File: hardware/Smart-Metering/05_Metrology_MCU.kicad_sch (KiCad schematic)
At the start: 26 parts, among them J501 SWD, U501 STM32F413RHT6, Y501 8MHz, Y502 32.768kHz

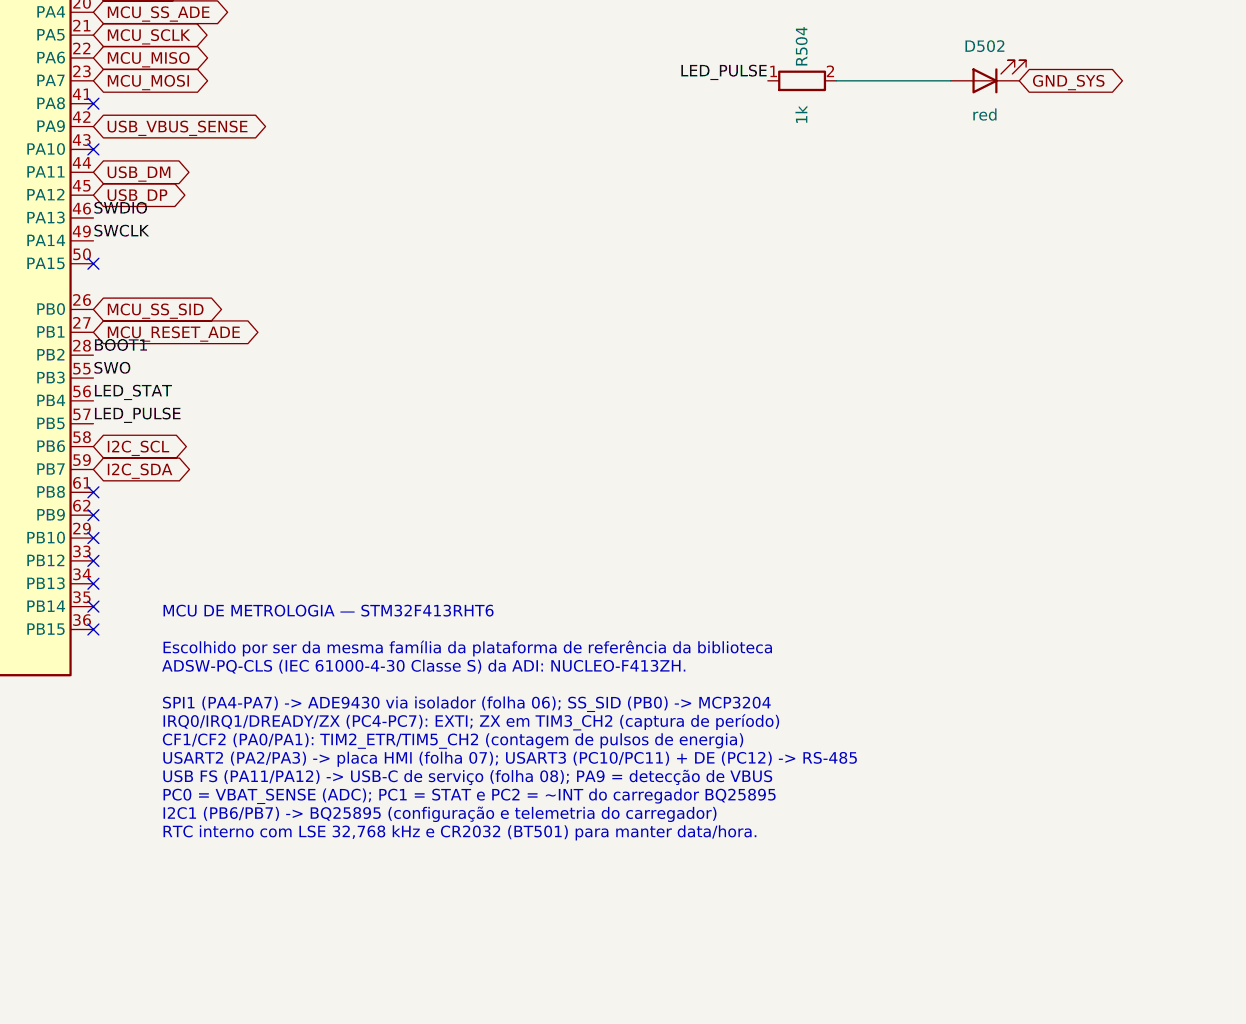
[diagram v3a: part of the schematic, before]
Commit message: Resolve as pendências da revisão do esquemático
P1  ADE9430: footprint VQFN-40 6x6 com EP de 4,15 mm, compatível com as
    variantes CP-40 de 6x6 mm (EP de 3,9 a 4,7 mm).
P2  Confirmado no datasheet: MISO solto com SS alto (pull-up de 100 kΩ)
    e NC1/NC2 em GND, como já estava.
P3  J301-J304: headers JST PH de 4 vias cabeados até conectores M8
    fêmea de painel (à prova de toque).
P4  PS601 -> U606 ADuM6000 (isoPower 5 kVrms, símbolo oficial).
P5  PS101 -> RAC20-05SK/277 (85-305 VAC, 120-430 VDC, 20 W); fusíveis
    T500mA, R101 3 W, C101 10 uF/450 V; entrada do BQ25895 a 3 A.
P7  TPS61089 -> TPS61022 (compensação interna, sem valores a ajustar).
P8  Placa EV alimentada pelos pinos 5 V do J1 (nota na folha 07).
P9  EEPROM de calibração 24LC64 no I2C1.
P10 Labels globais de uma só folha convertidos em locais.

Verificação: 223 componentes, nenhum pino solto, nenhuma net sem fonte,
nenhum conflito de saída, isolação íntegra, todos os footprints
existentes na biblioteca oficial do KiCad.

Co-Authored-By: Claude Opus 5.5 <noreply@anthropic.com>
Claude-Session: https://claude.ai/code/session_012B8cVkhtjf3eg98UdpNCpf
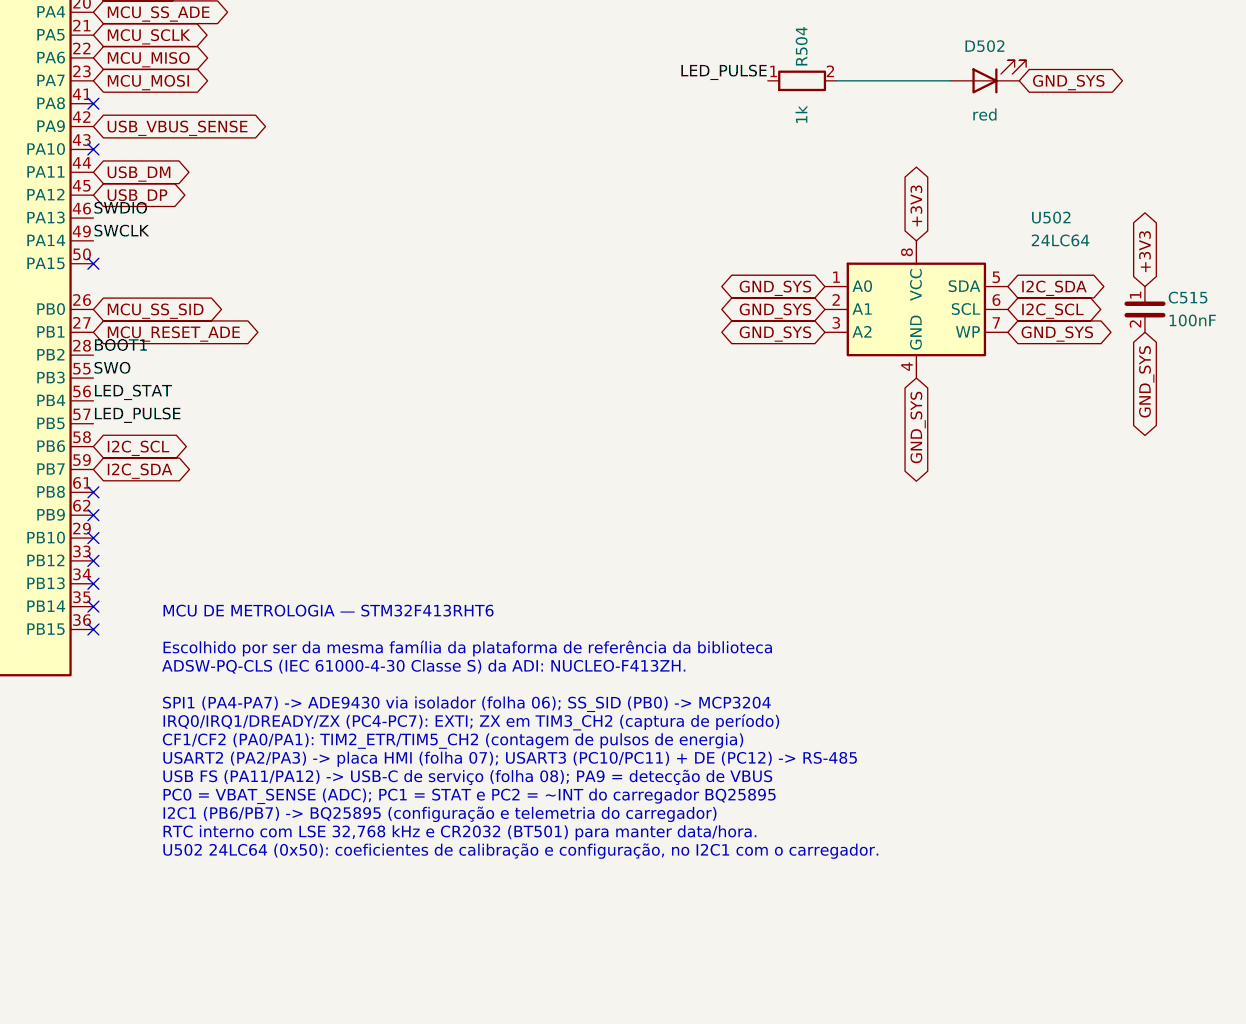
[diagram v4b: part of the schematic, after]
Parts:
- added C515: 100nF, Capacitor_SMD:C_0603_1608Metric, symbol SmartMetering:C_Vert
- added U502: 24LC64, Package_SO:SOIC-8_3.9x4.9mm_P1.27mm, symbol Memory_EEPROM:24LC64
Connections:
- net +3V3: now also C515.1, U502.8 (VCC)
- net GND_SYS: now also C515.2, U502.1 (A0), U502.2 (A1), U502.3 (A2), U502.4 (GND), U502.7 (WP)
- net I2C_SCL: now also U502.6 (SCL)
- net I2C_SDA: now also U502.5 (SDA)
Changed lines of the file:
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@@
 		(comment 2 "Platform matches the ADSW-PQ-CLS reference (NUCLEO-F413ZH)")
 	)
-	(text "MCU DE METROLOGIA — STM32F413RHT6\n\nEscolhido por ser da mesma família da plataforma de referência da biblioteca\nADSW-PQ-CLS (IEC 61000-4-30 Classe S) da ADI: NUCLEO-F413ZH.\n\nSPI1 (PA4-PA7) -> ADE9430 via isolador (folha 06); SS_SID (PB0) -> MCP3204\nIRQ0/IRQ1/DREADY/ZX (PC4-PC7): EXTI; ZX em TIM3_CH2 (captura de período)\nCF1/CF2 (PA0/PA1): TIM2_ETR/TIM5_CH2 (contagem de pulsos de energia)\nUSART2 (PA2/PA3) -> placa HMI (folha 07); USART3 (PC10/PC11) + DE (PC12) -> RS-485\nUSB FS (PA11/PA12) -> USB-C de serviço (folha 08); PA9 = detecção de VBUS\nPC0 = VBAT_SENSE (ADC); PC1 = STAT e PC2 = ~INT do carregador BQ25895\nI2C1 (PB6/PB7) -> BQ25895 (configuração e telemetria do carregador)\nRTC interno com LSE 32,768 kHz e CR2032 (BT501) para manter data/hora."
+	(text "MCU DE METROLOGIA — STM32F413RHT6\n\nEscolhido por ser da mesma família da plataforma de referência da biblioteca\nADSW-PQ-CLS (IEC 61000-4-30 Classe S) da ADI: NUCLEO-F413ZH.\n\nSPI1 (PA4-PA7) -> ADE9430 via isolador (folha 06); SS_SID (PB0) -> MCP3204\nIRQ0/IRQ1/DREADY/ZX (PC4-PC7): EXTI; ZX em TIM3_CH2 (captura de período)\nCF1/CF2 (PA0/PA1): TIM2_ETR/TIM5_CH2 (contagem de pulsos de energia)\nUSART2 (PA2/PA3) -> placa HMI (folha 07); USART3 (PC10/PC11) + DE (PC12) -> RS-485\nUSB FS (PA11/PA12) -> USB-C de serviço (folha 08); PA9 = detecção de VBUS\nPC0 = VBAT_SENSE (ADC); PC1 = STAT e PC2 = ~INT do carregador BQ25895\nI2C1 (PB6/PB7) -> BQ25895 (configuração e telemetria do carregador)\nRTC interno com LSE 32,768 kHz e CR2032 (BT501) para manter data/hora.\nU502 24LC64 (0x50): coeficientes de calibração e configuração, no I2C1 com o carregador."
 		(exclude_from_sim no)(at 180.34 175.26 0)
 		(effects (font (size 1.27 1.27)) (justify left top))
@@
 		(effects (font (size 1.27 1.27)) (justify left))
 		(property "Intersheetrefs" "${INTERSHEET_REFS}" (at 275.59 116.84 0) (hide yes) (effects (font (size 1.27 1.27))))
+	)
+	(global_label "GND_SYS" (shape bidirectional) (at 254 139.7 180)
+		(effects (font (size 1.27 1.27)) (justify right))
+		(property "Intersheetrefs" "${INTERSHEET_REFS}" (at 254 139.7 0) (hide yes) (effects (font (size 1.27 1.27))))
+	)
+	(global_label "GND_SYS" (shape bidirectional) (at 254 142.24 180)
+		(effects (font (size 1.27 1.27)) (justify right))
+		(property "Intersheetrefs" "${INTERSHEET_REFS}" (at 254 142.24 0) (hide yes) (effects (font (size 1.27 1.27))))
+	)
+	(global_label "GND_SYS" (shape bidirectional) (at 254 144.78 180)
+		(effects (font (size 1.27 1.27)) (justify right))
+		(property "Intersheetrefs" "${INTERSHEET_REFS}" (at 254 144.78 0) (hide yes) (effects (font (size 1.27 1.27))))
+	)
+	(global_label "GND_SYS" (shape bidirectional) (at 264.16 149.86 270)
+		(effects (font (size 1.27 1.27)) (justify right))
+		(property "Intersheetrefs" "${INTERSHEET_REFS}" (at 264.16 149.86 0) (hide yes) (effects (font (size 1.27 1.27))))
+	)
+	(global_label "GND_SYS" (shape bidirectional) (at 274.32 144.78 0)
+		(effects (font (size 1.27 1.27)) (justify left))
+		(property "Intersheetrefs" "${INTERSHEET_REFS}" (at 274.32 144.78 0) (hide yes) (effects (font (size 1.27 1.27))))
+	)
+	(global_label "+3V3" (shape bidirectional) (at 264.16 134.62 90)
+		(effects (font (size 1.27 1.27)) (justify left))
+		(property "Intersheetrefs" "${INTERSHEET_REFS}" (at 264.16 134.62 0) (hide yes) (effects (font (size 1.27 1.27))))
+	)
+	(global_label "I2C_SDA" (shape bidirectional) (at 274.32 139.7 0)
+		(effects (font (size 1.27 1.27)) (justify left))
+		(property "Intersheetrefs" "${INTERSHEET_REFS}" (at 274.32 139.7 0) (hide yes) (effects (font (size 1.27 1.27))))
+	)
+	(global_label "I2C_SCL" (shape bidirectional) (at 274.32 142.24 0)
+		(effects (font (size 1.27 1.27)) (justify left))
+		(property "Intersheetrefs" "${INTERSHEET_REFS}" (at 274.32 142.24 0) (hide yes) (effects (font (size 1.27 1.27))))
+	)
+	(global_label "+3V3" (shape bidirectional) (at 289.56 139.7 90)
+		(effects (font (size 1.27 1.27)) (justify left))
+		(property "Intersheetrefs" "${INTERSHEET_REFS}" (at 289.56 139.7 0) (hide yes) (effects (font (size 1.27 1.27))))
+	)
+	(global_label "GND_SYS" (shape bidirectional) (at 289.56 144.78 270)
+		(effects (font (size 1.27 1.27)) (justify right))
+		(property "Intersheetrefs" "${INTERSHEET_REFS}" (at 289.56 144.78 0) (hide yes) (effects (font (size 1.27 1.27))))
 	)
 	(symbol
@@
 			)
 		)
+	)
+	(symbol
+		(lib_id "Memory_EEPROM:24LC64")
+		(at 264.16 142.24 0)
+		(unit 1)(body_style 1)
+		(exclude_from_sim no)(in_bom yes)(on_board yes)(in_pos_files yes)(dnp no)
+		(property "Reference" "U502" (at 276.86 132.08 0) (effects (font (size 1.27 1.27)) (justify left)))
+		(property "Value" "24LC64" (at 276.86 134.62 0) (effects (font (size 1.27 1.27)) (justify left)))
+		(property "Footprint" "Package_SO:SOIC-8_3.9x4.9mm_P1.27mm" (at 264.16 142.24 0) (effects (font (size 1.27 1.27)) (hide yes)))
+		(property "Datasheet" "" (at 264.16 142.24 0) (effects (font (size 1.27 1.27)) (hide yes)))
+		(property "Description" "Calibration / configuration EEPROM, 64 kbit" (at 264.16 142.24 0) (effects (font (size 1.27 1.27)) (hide yes)))
+		(pin "1")
+		(pin "2")
+		(pin "3")
+		(pin "4")
+		(pin "5")
+		(pin "6")
+		(pin "7")
+		(pin "8")
+		(instances
+			(project "Smart-Metering"
+				(path "/5fa62d70-4279-48bb-8603-6bcc60fb353a/a10e1005-0005-4e05-9005-000000000005" (reference "U502") (unit 1))
+			)
+		)
+	)
+	(symbol
+		(lib_id "SmartMetering:C_Vert")
+		(at 289.56 142.24 0)
+		(unit 1)(body_style 1)
+		(exclude_from_sim no)(in_bom yes)(on_board yes)(in_pos_files yes)(dnp no)
+		(property "Reference" "C515" (at 292.1 140.97 0) (effects (font (size 1.27 1.27)) (justify left)))
+		(property "Value" "100nF" (at 292.1 143.51 0) (effects (font (size 1.27 1.27)) (justify left)))
+		(property "Footprint" "Capacitor_SMD:C_0603_1608Metric" (at 289.56 142.24 0) (effects (font (size 1.27 1.27)) (hide yes)))
+		(property "Datasheet" "" (at 289.56 142.24 0) (effects (font (size 1.27 1.27)) (hide yes)))
+		(property "Description" "EEPROM decoupling" (at 289.56 142.24 0) (effects (font (size 1.27 1.27)) (hide yes)))
+		(pin "1")
+		(pin "2")
+		(instances
+			(project "Smart-Metering"
+				(path "/5fa62d70-4279-48bb-8603-6bcc60fb353a/a10e1005-0005-4e05-9005-000000000005" (reference "C515") (unit 1))
+			)
+		)
